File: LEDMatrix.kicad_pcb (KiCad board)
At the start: 2 copper layers, 33.8 x 131 mm, 75 parts, among them J1 Conn_02x04_Odd_Even, SW2 SW_Push, U1 W25Q16JVUXIQ, U10 VDMR10A1, U11 VDMR10A1, U12 VDMR10A1, U2 RP2040, U3 IS31FL3729-QFLS4-TR, U4 VDMR10A1, U5 VDMR10A1, U6 VDMR10A1, U7 VDMR10A1, U8 VDMR10A1, U9 VDMR10A1, Y1 12.000MHz

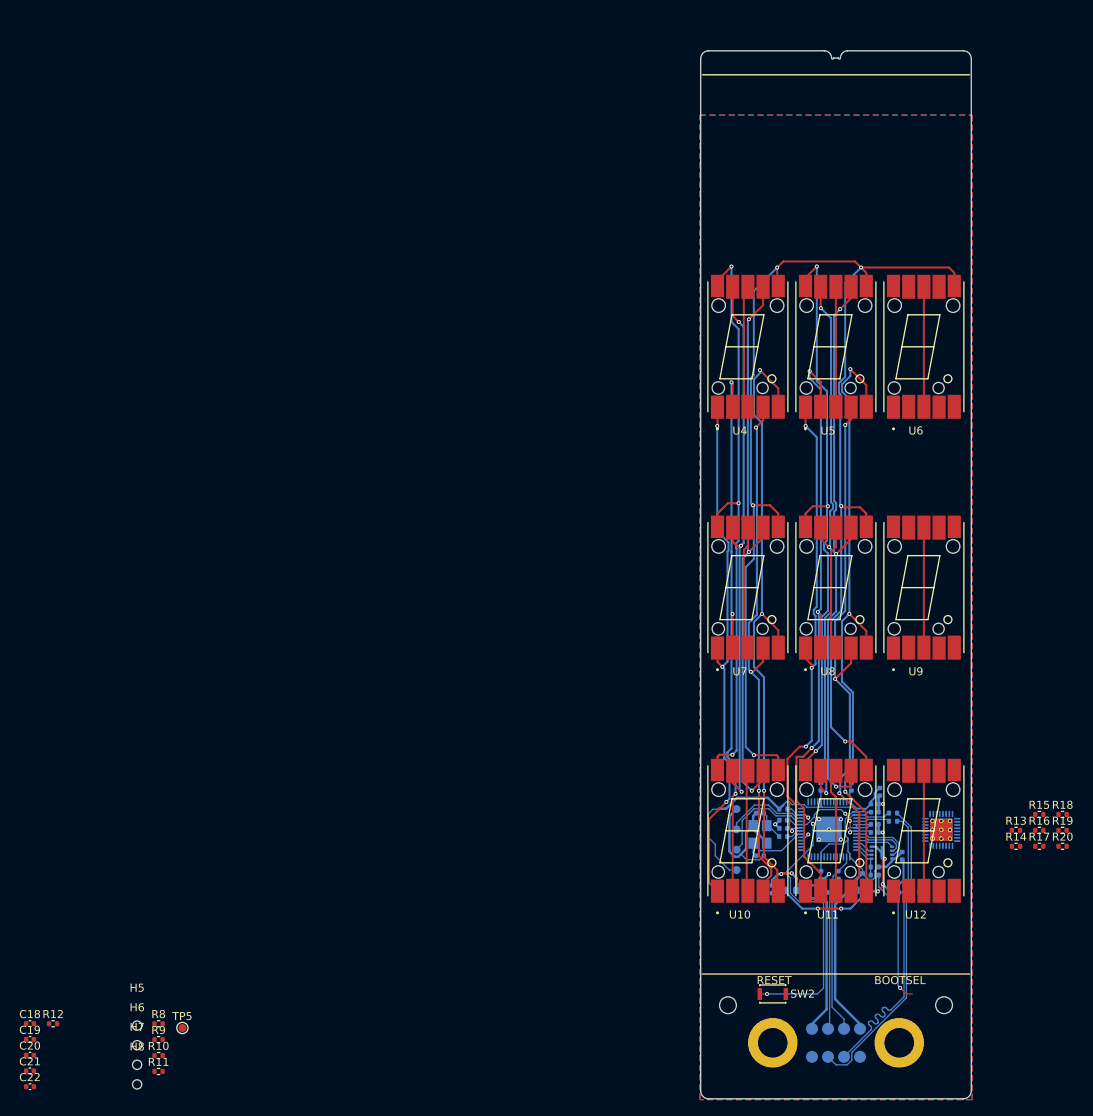
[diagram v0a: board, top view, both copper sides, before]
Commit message: Routing complete but not DRC clean
Also want to add 3-9 neopixels here to backlight the legend.
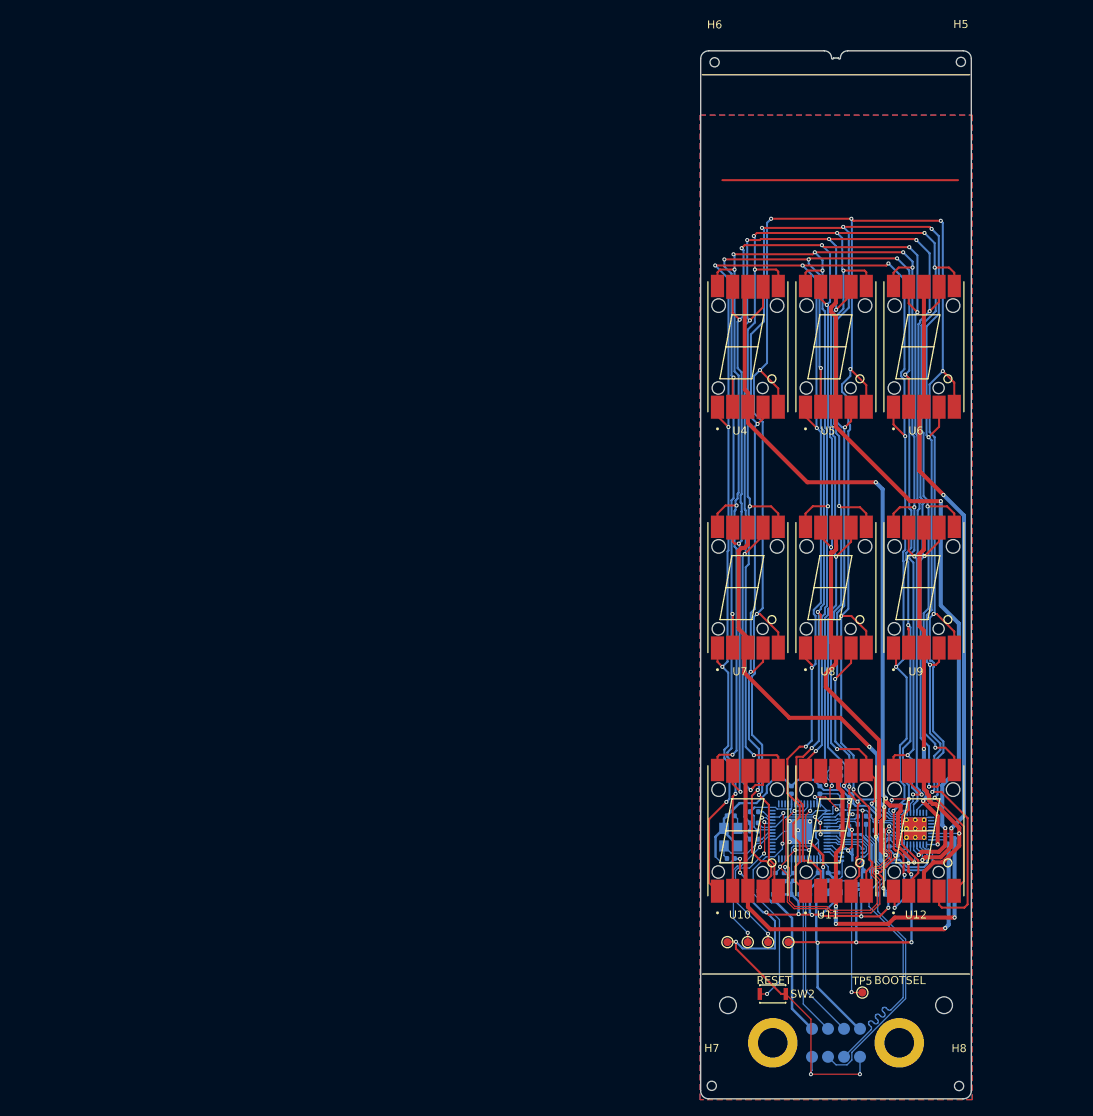
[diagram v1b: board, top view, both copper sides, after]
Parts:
- removed C20, C22: 100nF, Capacitor_SMD:C_0402_1005Metric
- removed C21: 1uF, Capacitor_SMD:C_0402_1005Metric
- removed R11: 100k, Resistor_SMD:R_0402_1005Metric
- removed R13, R14, R15, R16, R17, R18, R19, R20: 20, Resistor_SMD:R_0402_1005Metric
- C18, R10, R12, R8, R9: moved to B.Cu
- C19: value 1uF -> 100nF; moved to B.Cu
- TP1, TP2, TP3, TP4: moved to F.Cu
- moved H5 158.5 mm to (82.5, 51.4)
- moved H6 142.5 mm to (51.7, 51.4)
- moved C18 109.8 mm to (73.6, 149.0), turned to 90 degrees
- moved C19 106.7 mm to (67.5, 140.1), turned to -90 degrees
- moved R12 106.0 mm to (72.3, 147.4), turned to 180 degrees
- moved H8 102.7 mm to (82.3, 179.4)
- moved R9 90.5 mm to (66.3, 140.1), turned to -90 degrees
- moved TP5 85.1 mm to (70.2, 167.7)
- moved R10 81.3 mm to (60.5, 153.3), turned to 90 degrees
- moved R8 79.3 mm to (59.3, 153.3), turned to 90 degrees
- moved H7 71.9 mm to (51.4, 179.4)
- moved C17 16.7 mm to (75.1, 150.5), turned to 180 degrees
- moved TP4 16.7 mm to (53.3, 161.4), turned to 90 degrees
- moved TP3 14.2 mm to (55.9, 161.4), turned to 90 degrees
- moved TP2 12.2 mm to (58.4, 161.4), turned to 90 degrees
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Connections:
- C14 pad 1: /SDB -> +3V3
- C17 pad 1: +5V -> +3V3
- C18 pad 1: +5V -> +3V3
- C19 pad 1: +5V -> /SDB
- U2 pad 40: /INTB -> unconnected-(U2-GPIO28_ADC2-Pad40)
- U3 pad 1: Net-(U3-CS4) -> /Driver/CS3
- U3 pad 2: Net-(U3-CS5) -> /Driver/CS4
- U3 pad 23: +5V -> +3V3
- U3 pad 3: Net-(U3-CS6) -> /Driver/CS5
- U3 pad 30: Net-(U3-CS1) -> /Driver/CS0
- U3 pad 31: Net-(U3-CS2) -> /Driver/CS1
- U3 pad 32: Net-(U3-CS3) -> /Driver/CS2
- U3 pad 33: (no net) -> GND
- U3 pad 4: Net-(U3-CS7) -> /Driver/CS6
- U3 pad 5: Net-(U3-CS8) -> /Driver/CS7
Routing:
- net /Driver/CS2: track 135.5 -> 318.7 mm, vias 6 -> 13
- net /Driver/CS7: track 157.1 -> 321.2 mm, vias 6 -> 12
- net /Driver/CS4: track 132.8 -> 295.7 mm, vias 6 -> 14
- net /Driver/CS3: track 149.9 -> 298.8 mm, vias 6 -> 13
- net /Driver/CS0: track 143.9 -> 276.5 mm, vias 6 -> 12
- net /Driver/CS5: track 140.7 -> 261.3 mm, vias 6 -> 13
- net GND: track 62.8 -> 176.6 mm, vias 15 -> 24
- net /Driver/CS6: track 146.4 -> 257.4 mm, vias 6 -> 12
- net /Driver/CS1: track 175.0 -> 275.6 mm, vias 6 -> 13
- net /Driver/LED_SW0: track 15.4 -> 89.5 mm, vias 0 -> 3
- net /Driver/LED_SW1: track 15.0 -> 85.3 mm, vias 0 -> 3
- net /Driver/LED_SW2: track 15.0 -> 79.8 mm, vias 0 -> 3
- net /Driver/LED_SW3: track 15.4 -> 62.4 mm, vias 0 -> 3
- net /Driver/LED_SW6: track 15.1 -> 56.3 mm, vias 0 -> 1
- net /Driver/LED_SW4: track 15.5 -> 56.6 mm, vias 0 -> 1
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
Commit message: Finished version w/ legend on silkscreen, DRC clean
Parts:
- R7: value 330k -> 180k
- moved SW2 8.00 mm to (53.1, 173.3)
- moved TP1 5.59 mm to (60.2, 167.0)
- moved TP2 5.59 mm to (57.7, 167.0)
- moved TP3 5.59 mm to (55.1, 167.0)
- moved TP4 5.59 mm to (52.6, 167.0)
- moved D4 0.23 mm to (72.8, 155.4)
- moved C11 0.23 mm to (65.1, 142.4)
- moved D1 0.15 mm to (64.0, 155.4)
- moved R1 0.10 mm to (69.2, 154.2)
- moved C16 0.05 mm to (66.6, 155.2)
- moved D3 0.05 mm to (70.5, 155.4)
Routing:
- net GND: track 176.6 -> 280.1 mm, vias 24 -> 47
- net (no net): track 29.5 -> 0.00 mm
- net /RUN: track 31.3 -> 38.8 mm
- net /SWD: track 19.5 -> 26.4 mm
- net /Driver/CS2: track 318.7 -> 312.0 mm
- net /SWCLK: track 20.1 -> 26.7 mm
- net /SDB: track 26.5 -> 20.2 mm, vias 4 -> 3
- net /Driver/LED_SW5: track 42.6 -> 47.2 mm
- net /Driver/CS0: track 276.5 -> 272.3 mm
- net +3V3: track 118.5 -> 122.2 mm
- net /Driver/CS5: track 261.3 -> 257.7 mm
- net /Driver/CS1: track 275.6 -> 272.8 mm
- net /Driver/CS4: track 295.7 -> 298.1 mm
- net /Driver/LED_SW1: track 85.3 -> 87.5 mm
- net /Driver/CS7: track 321.2 -> 319.4 mm
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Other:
- board text added: "1"
- board text added: "JLCJLCJLCJLC"

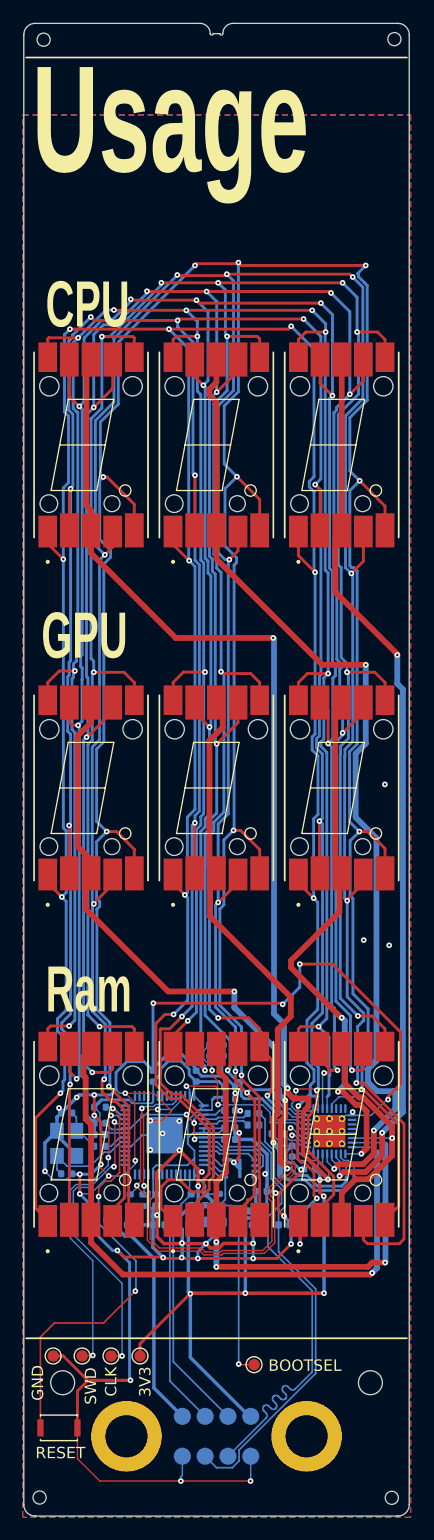
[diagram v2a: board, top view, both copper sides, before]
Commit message: Version 2, with right angle neopixel backlighting
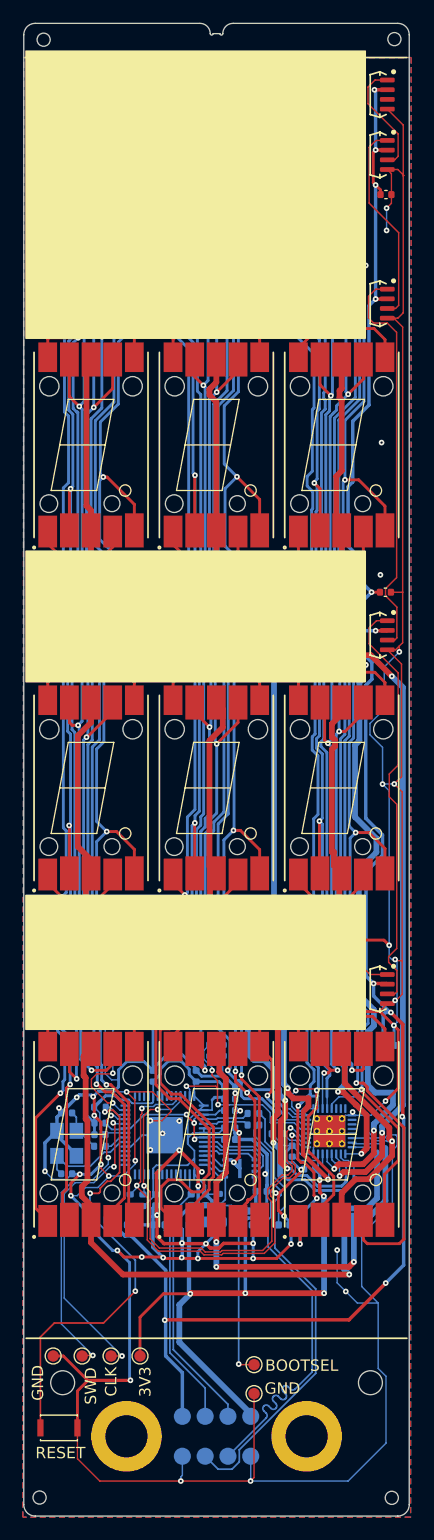
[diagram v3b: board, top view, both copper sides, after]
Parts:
- added C20: 100nF, Capacitor_SMD:C_0402_1005Metric, B.Cu at (82.0, 139.7)
- added C21: 100nF, Capacitor_SMD:C_0402_1005Metric, F.Cu at (81.8, 65.0)
- added C22: 100nF, Capacitor_SMD:C_0402_1005Metric, F.Cu at (81.7, 99.9)
- added D10: WS2812B-4020, LEDMatrix:WS2812B-4020, F.Cu at (81.2, 56.2)
- added D6: WS2812B-4020, LEDMatrix:WS2812B-4020, F.Cu at (81.2, 134.8)
- added D7: WS2812B-4020, LEDMatrix:WS2812B-4020, F.Cu at (81.2, 103.7)
- added D8: WS2812B-4020, LEDMatrix:WS2812B-4020, F.Cu at (81.2, 74.6)
- added D9: WS2812B-4020, LEDMatrix:WS2812B-4020, F.Cu at (81.2, 61.5)
- added TP6: GND, TestPoint:TestPoint_Pad_D1.0mm, F.Cu at (70.2, 170.3)
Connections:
- U2 pad 27: unconnected-(U2-GPIO16-Pad27) -> /NEOPIXEL
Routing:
- net GND: track 280.1 -> 501.7 mm, vias 47 -> 60
- net +5V: track 21.3 -> 164.9 mm, vias 0 -> 11
- net /NEOPIXEL: track 0.00 -> 38.2 mm, vias 0 -> 5
- net Net-(D6-DO): track 0.00 -> 36.9 mm
- net Net-(D7-DO): track 0.00 -> 35.3 mm
- net Net-(D8-DO): track 0.00 -> 17.9 mm
- net Net-(D10-DIN): track 0.00 -> 10.2 mm
- net +3V3: track 122.2 -> 124.6 mm
- net /RUN: track 38.8 -> 40.8 mm
- net /Driver/LED_SW2: track 80.1 -> 81.7 mm
- net /Driver/CS1: track 272.8 -> 274.1 mm
- net /Driver/LED_SW6: track 56.6 -> 57.7 mm
- net /SWD: track 26.4 -> 27.4 mm
- net /SWCLK: track 26.7 -> 27.7 mm
- net /Driver/LED_SW1: track 87.5 -> 88.5 mm
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
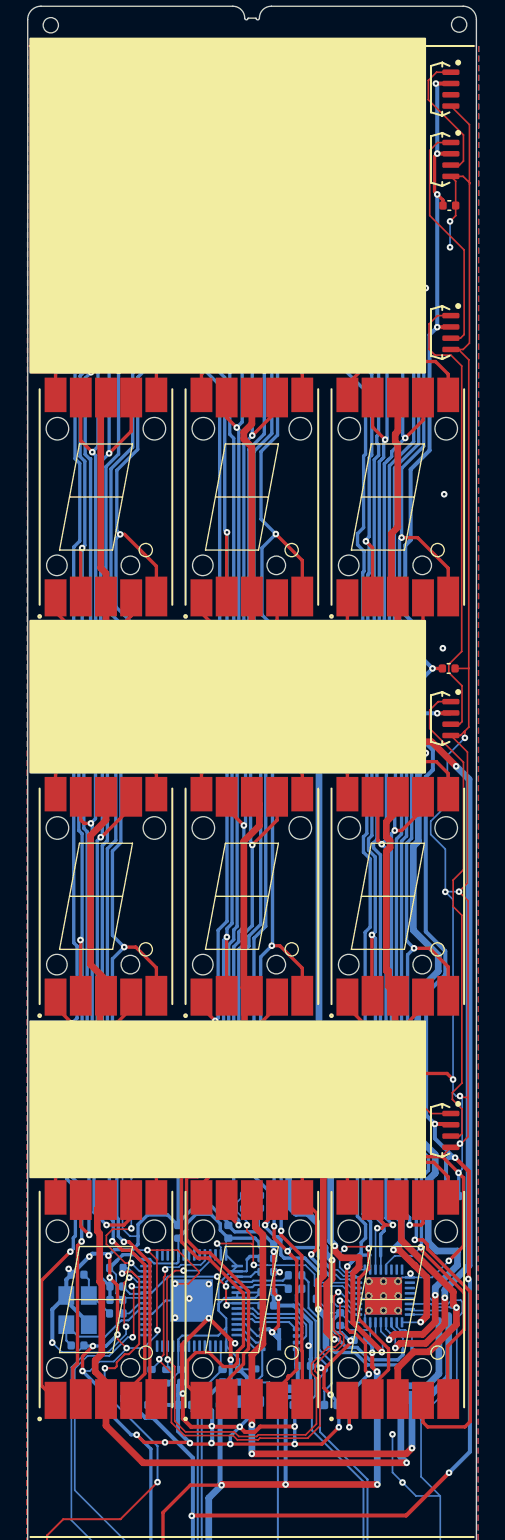
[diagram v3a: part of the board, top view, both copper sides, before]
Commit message: Tweaks from JLCDFM tools, mostly moving vias away from pads
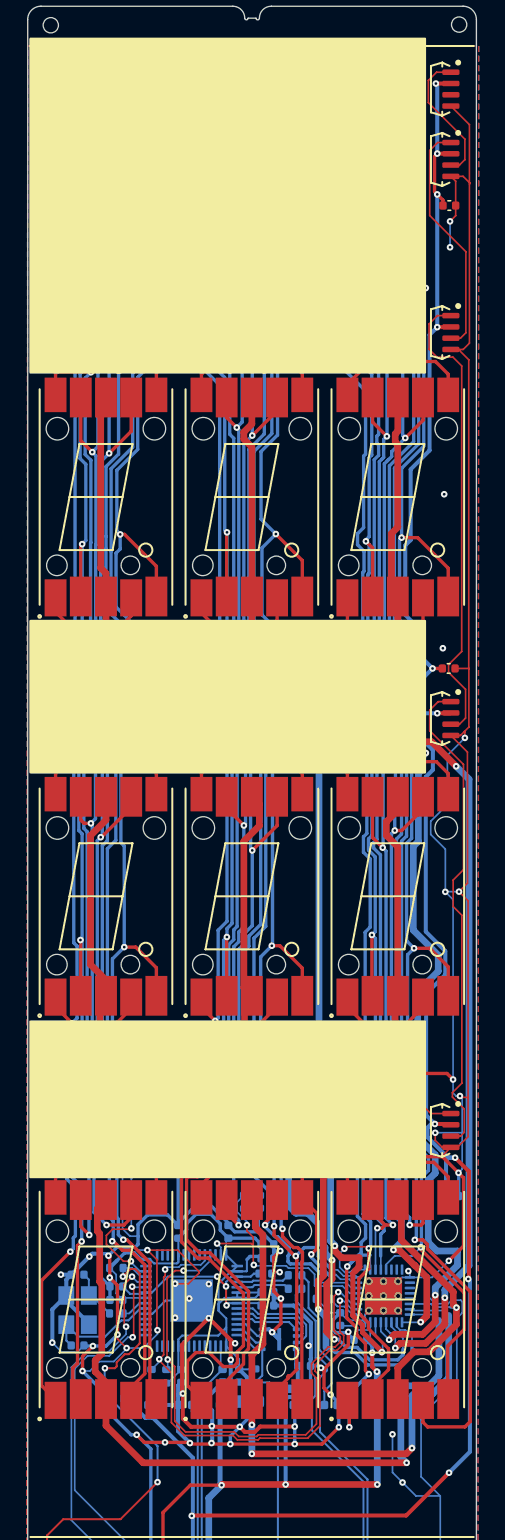
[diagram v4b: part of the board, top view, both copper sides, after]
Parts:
- C1, C2: value 15pF -> 22pF
- moved C6 0.20 mm to (67.9, 145.5)
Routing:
- net GND: track 501.7 -> 507.6 mm
- net +5V: track 164.9 -> 165.8 mm
- net /Driver/LED_SW7: track 48.0 -> 47.2 mm
- net /Driver/CS2: track 312.1 -> 311.3 mm
- net /RUN: track 40.8 -> 41.4 mm

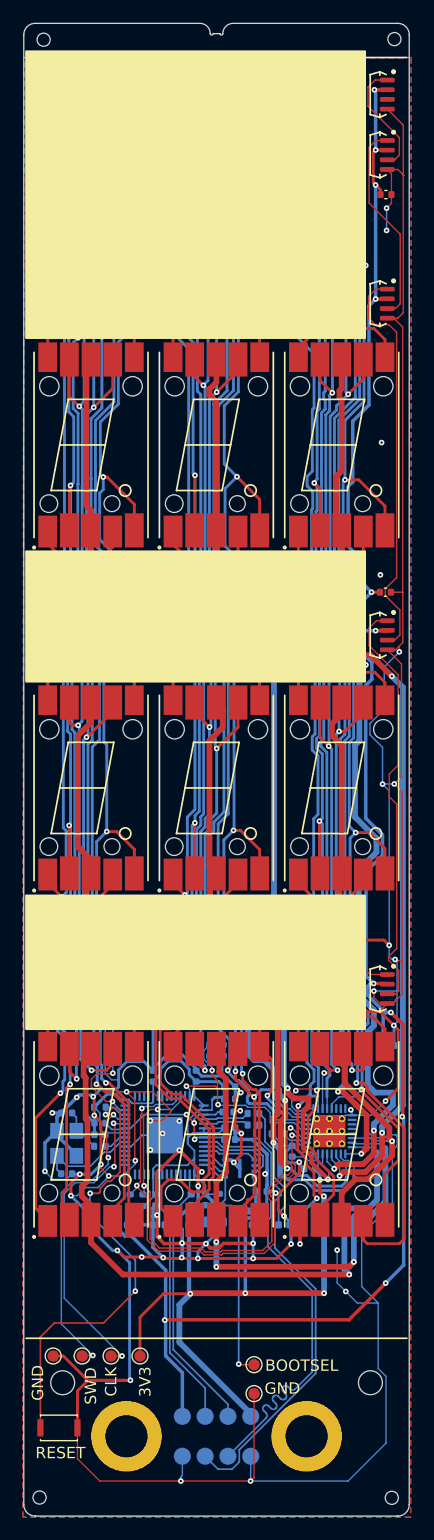
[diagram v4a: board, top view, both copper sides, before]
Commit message: Another update before sending to JLCPCB
1. Narrowed the spacing between the LED displays
2. Made the position of the neopixels more consistent
3. Extended the silkscreen up a bit
4. Added my name to the front of the board
5. Designed the enclosure grid
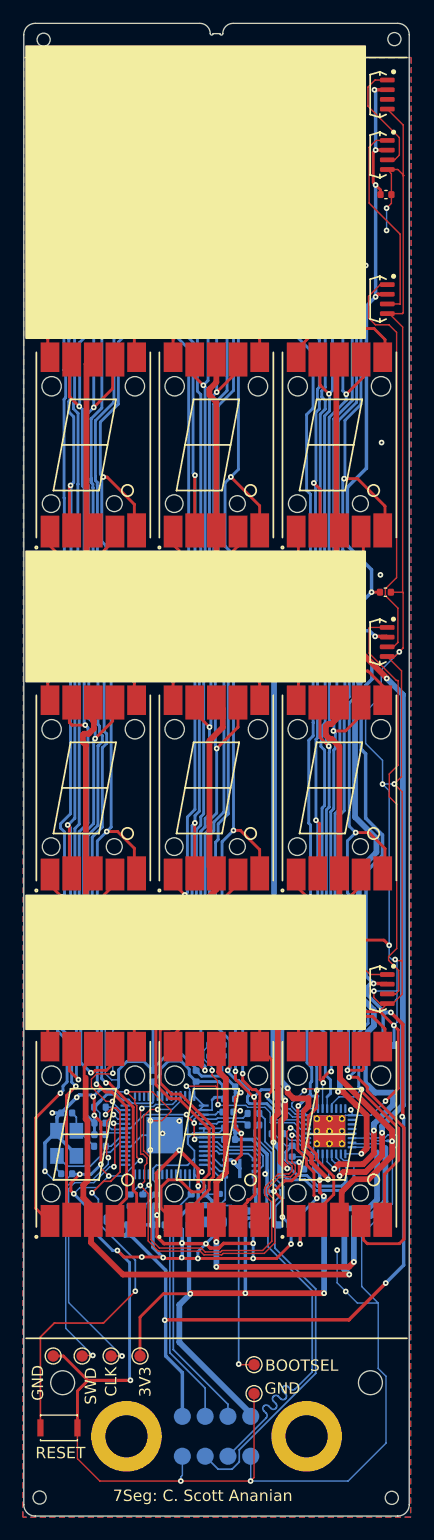
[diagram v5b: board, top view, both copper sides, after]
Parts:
- R12: value 18k -> 33k
- moved D7 0.59 mm to (81.2, 104.3)
- moved D8 0.40 mm to (81.2, 74.2)
- moved U10 0.20 mm to (56.1, 147.5)
- moved U12 0.20 mm to (77.7, 147.5)
- moved U4 0.20 mm to (56.1, 87.0)
- moved U6 0.20 mm to (77.7, 87.0)
- moved U7 0.20 mm to (56.1, 117.1)
- moved U9 0.20 mm to (77.7, 117.1)
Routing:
- net /Driver/CS0: track 272.8 -> 274.8 mm
- net /Driver/CS2: track 311.3 -> 313.1 mm
- net /Driver/CS5: track 257.9 -> 259.5 mm
- net /Driver/LED_SW2: track 81.7 -> 80.1 mm
- net /I2C1_SDA: track 41.5 -> 42.5 mm
- net /Driver/LED_SW3: track 62.5 -> 61.7 mm
- net /Driver/CS4: track 297.6 -> 298.5 mm
- net /Driver/CS7: track 319.2 -> 318.4 mm
- net /I2C1_SCL: track 41.0 -> 41.8 mm
- net +5V: track 165.8 -> 166.5 mm
- net Net-(D7-DO): track 35.6 -> 36.1 mm
- net /Driver/CS3: track 300.2 -> 300.7 mm
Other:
- board text added: "7Seg: C. Scott Ananian"
